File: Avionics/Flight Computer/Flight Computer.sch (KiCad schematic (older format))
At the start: 24 parts, among them U6 LP5521YQ

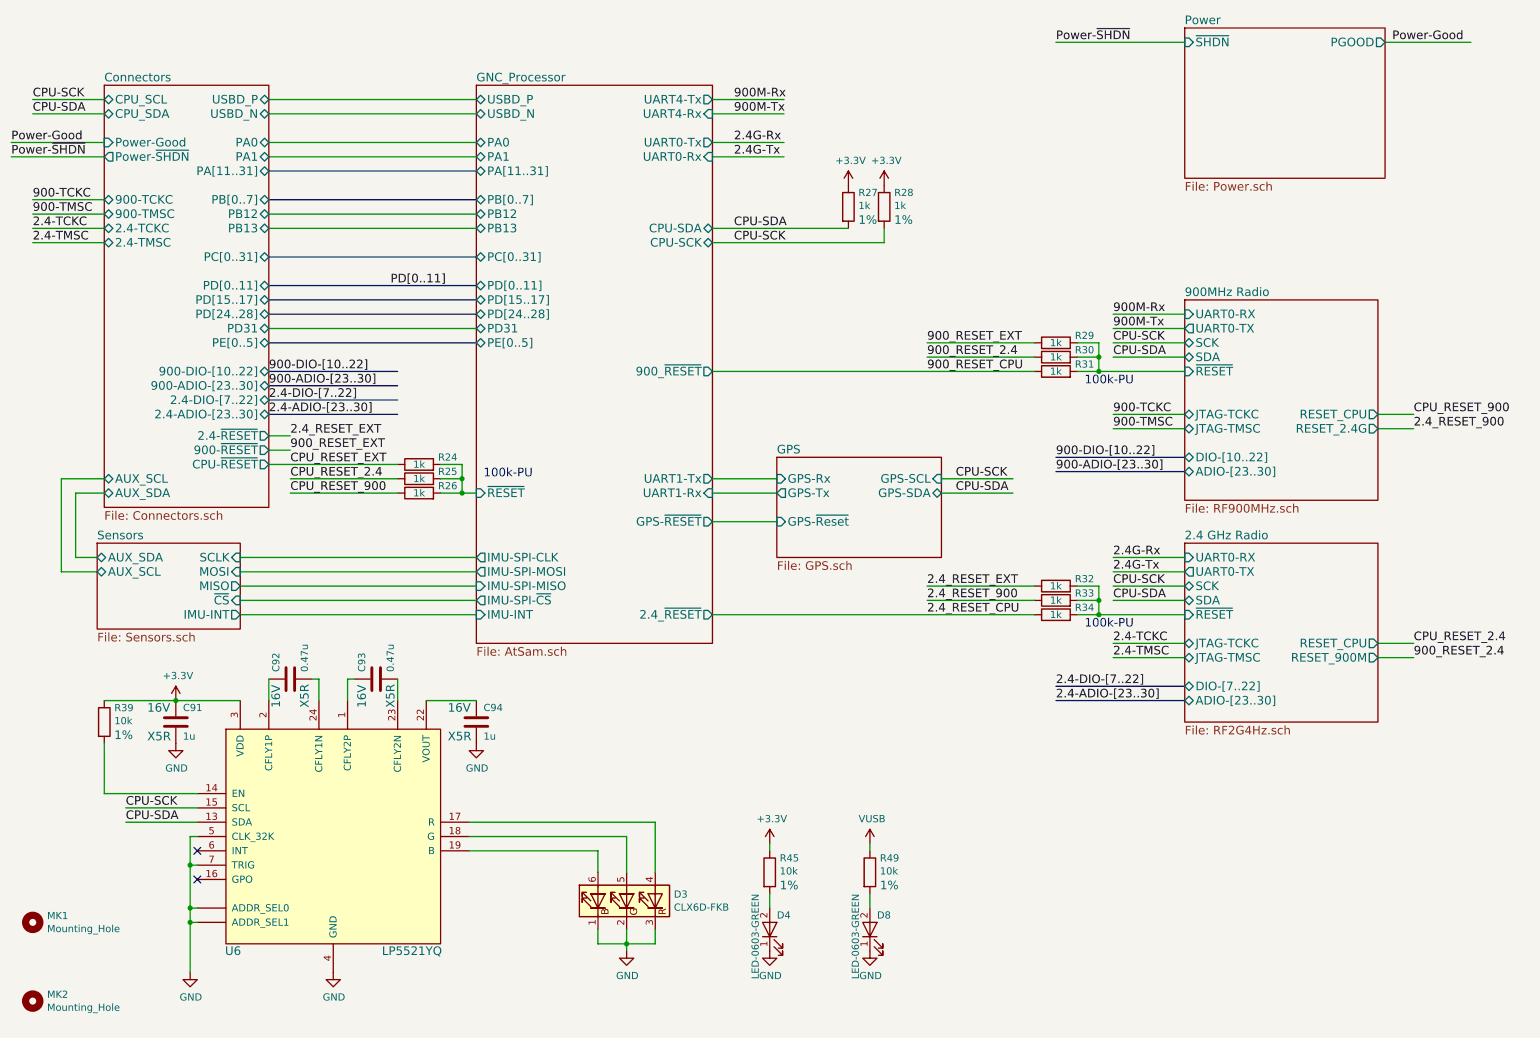
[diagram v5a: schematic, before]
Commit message: Added option resistors for IMU to be connected to radio chips via I2C
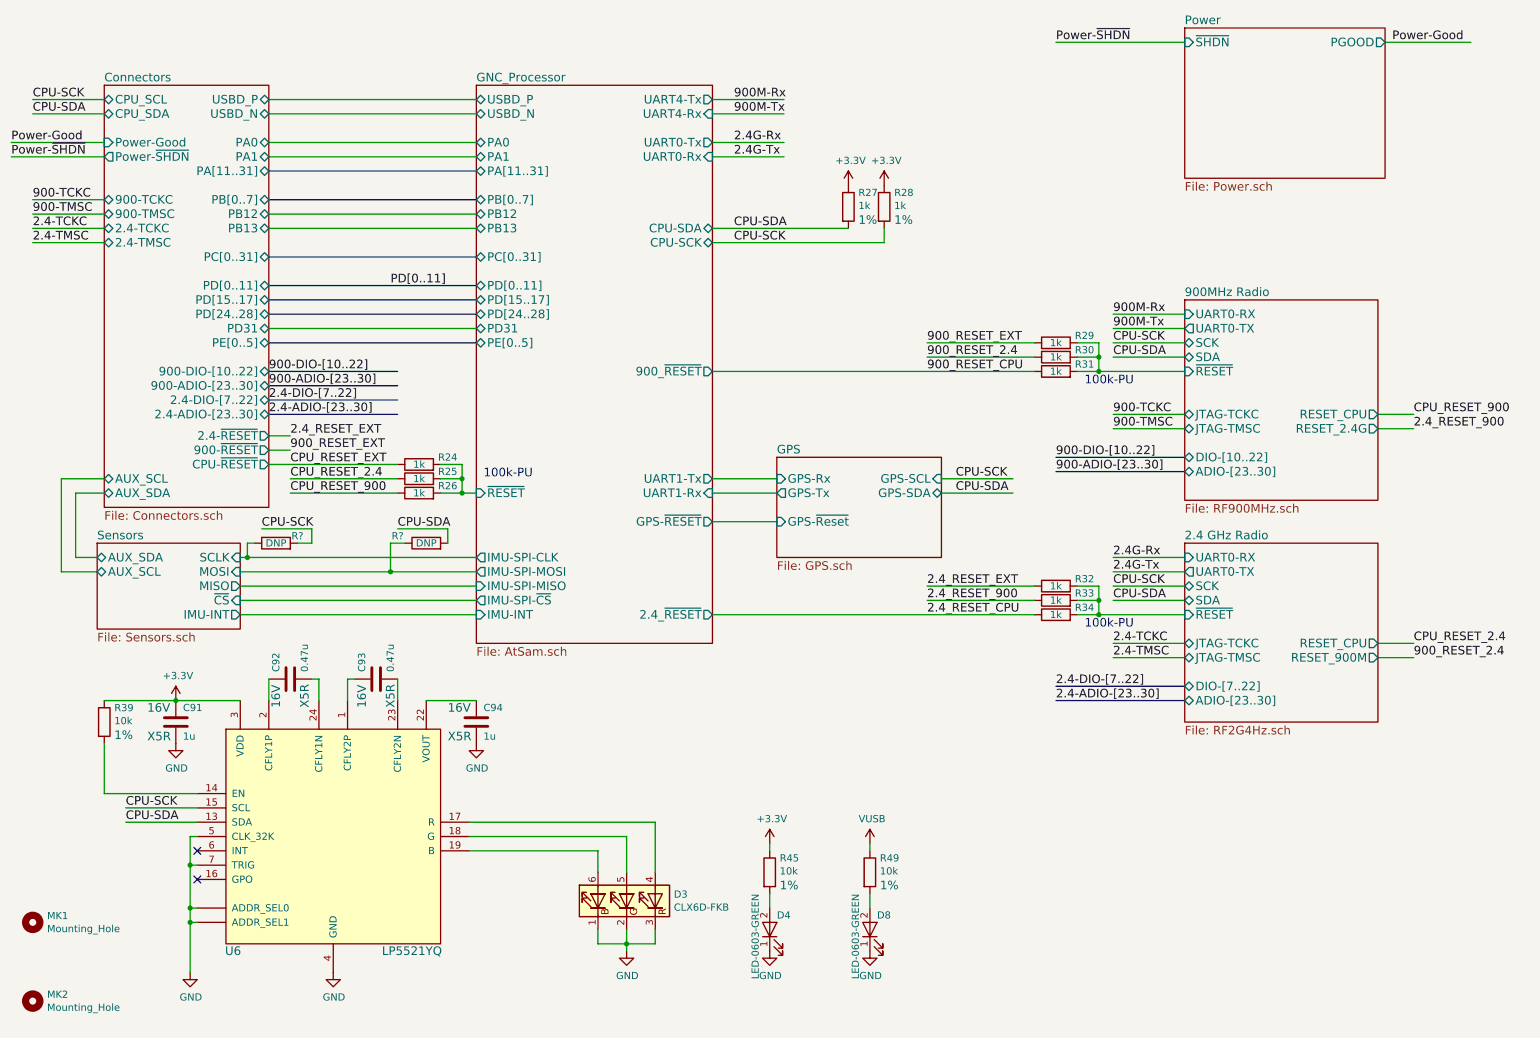
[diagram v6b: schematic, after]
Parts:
- added R? (x2): DNP, Resistors_SMD:R_0402, symbol R
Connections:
- wire segments 110 -> 133
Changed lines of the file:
@@
 	5450 2300 6650 2300
 Wire Wire Line
-	2150 4500 3800 4500
-Wire Wire Line
-	3800 4600 2150 4600
+	2150 4500 2200 4500
+Wire Wire Line
+	2200 4500 3800 4500
+Wire Wire Line
+	3800 4600 3200 4600
+Wire Wire Line
+	3200 4600 2150 4600
 Wire Wire Line
 	2150 4700 3800 4700
@@
 	6650 2300 6650 2200
 Wire Wire Line
-	3550 4050 3800 4050
+	3550 4050 3700 4050
+Wire Wire Line
+	3700 4050 3800 4050
 Wire Wire Line
 	3550 3950 3700 3950
 Wire Wire Line
-	3700 3850 3700 4050
+	3700 3850 3700 3950
+Wire Wire Line
+	3700 3950 3700 4050
 Connection ~ 3700 4050
 Wire Wire Line
@@
 	10100 5200 10350 5200
 Wire Wire Line
-	8000 4900 8750 4900
+	8000 4900 8150 4900
+Wire Wire Line
+	8150 4900 8750 4900
 Wire Wire Line
 	8000 4800 8150 4800
 Wire Wire Line
-	8150 4700 8150 4900
+	8150 4700 8150 4800
+Wire Wire Line
+	8150 4800 8150 4900
 Connection ~ 8150 4900
 Wire Wire Line
@@
 	7850 3900 8750 3900
 Wire Wire Line
-	8000 3200 8750 3200
+	8000 3200 8150 3200
+Wire Wire Line
+	8150 3200 8750 3200
 Wire Wire Line
 	8000 3100 8150 3100
 Wire Wire Line
-	8150 3000 8150 3200
+	8150 3000 8150 3100
+Wire Wire Line
+	8150 3100 8150 3200
 Connection ~ 8150 3200
 Wire Wire Line
@@
 	4650 7100 4650 7200
 Wire Wire Line
-	4650 7200 5050 7200
-Wire Wire Line
-	4850 7100 4850 7250
+	4650 7200 4850 7200
+Wire Wire Line
+	4850 7200 5050 7200
+Wire Wire Line
+	4850 7100 4850 7200
+Wire Wire Line
+	4850 7200 4850 7250
 Connection ~ 4850 7200
 Wire Wire Line
@@
 $EndComp
 Wire Wire Line
-	1200 5500 2150 5500
+	1200 5500 1700 5500
+Wire Wire Line
+	1700 5500 2150 5500
 $Comp
 L GND #PWR010
@@
 $EndComp
 Wire Wire Line
-	1800 6450 1800 7400
+	1800 6450 1800 6650
+Wire Wire Line
+	1800 6650 1800 6950
+Wire Wire Line
+	1800 6950 1800 7050
+Wire Wire Line
+	1800 7050 1800 7400
 Wire Wire Line
 	1800 6950 1850 6950
@@
 Wire Wire Line
 	7050 4050 7550 4050
+$Comp
+L R R?
+U 1 1 58D60CF9
+P 2400 4400
+F 0 "R?" V 2450 4250 50  0000 C CNN
+F 1 "DNP" V 2400 4400 50  0000 C CNN
+F 2 "Resistors_SMD:R_0402" V -5050 2750 50  0001 C CNN
+F 3 "" V -4770 2750 50  0001 C CNN
+F 4 "1%" V 2550 4700 60  0001 C CNN "Tolerance"
+F 5 "16V" V -4600 2750 60  0001 C CNN "Voltage"
+F 6 "0.062W" V -4500 2750 60  0001 C CNN "Power"
+F 7 "Thin Film" V -4400 2750 60  0001 C CNN "Material"
+F 8 "0402" V -4950 2750 60  0001 C CNN "Package"
+	1    2400 4400
+	0    -1   -1   0
+$EndComp
+$Comp
+L R R?
+U 1 1 58D60FCF
+P 3450 4400
+F 0 "R?" V 3500 4600 50  0000 C CNN
+F 1 "DNP" V 3450 4400 50  0000 C CNN
+F 2 "Resistors_SMD:R_0402" V -4000 2750 50  0001 C CNN
+F 3 "" V -3720 2750 50  0001 C CNN
+F 4 "1%" V 3600 4700 60  0001 C CNN "Tolerance"
+F 5 "16V" V -3550 2750 60  0001 C CNN "Voltage"
+F 6 "0.062W" V -3450 2750 60  0001 C CNN "Power"
+F 7 "Thin Film" V -3350 2750 60  0001 C CNN "Material"
+F 8 "0402" V -3900 2750 60  0001 C CNN "Package"
+	1    3450 4400
+	0    -1   -1   0
+$EndComp
+Wire Wire Line
+	2200 4500 2200 4400
+Wire Wire Line
+	2200 4400 2250 4400
+Connection ~ 2200 4500
+Wire Wire Line
+	3200 4600 3200 4400
+Wire Wire Line
+	3200 4400 3300 4400
+Connection ~ 3200 4600
+Wire Wire Line
+	3600 4400 3600 4300
+Wire Wire Line
+	3600 4300 3250 4300
+Wire Wire Line
+	2550 4400 2650 4400
+Wire Wire Line
+	2650 4400 2650 4300
+Wire Wire Line
+	2650 4300 2300 4300
+Text Label 2300 4300 0    60   ~ 0
+CPU-SCK
+Text Label 3250 4300 0    60   ~ 0
+CPU-SDA
 $EndSCHEMATC

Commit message: Added pullup to CS
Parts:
- added U10, U11: Logo, Symbols:NaviLOGO, symbol BOX1
- gave numbers to parts that had none: 2
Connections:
- wire segments 133 -> 119
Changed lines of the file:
@@
 $EndComp
 $Comp
-L +3.3V #PWR01
+L +3.3V #PWR12
 U 1 1 58BFF81C
 P 6650 1900
-F 0 "#PWR01" H 4950 -600 50  0001 C CNN
+F 0 "#PWR12" H 4950 -600 50  0001 C CNN
 F 1 "+3.3V" H 6665 2073 50  0000 C CNN
 F 2 "" H 4950 -450 50  0001 C CNN
@@
 $EndComp
 $Comp
-L +3.3V #PWR02
+L +3.3V #PWR9
 U 1 1 58BFF8E0
 P 6400 1900
-F 0 "#PWR02" H 4700 -600 50  0001 C CNN
+F 0 "#PWR9" H 4700 -600 50  0001 C CNN
 F 1 "+3.3V" H 6415 2073 50  0000 C CNN
 F 2 "" H 4700 -450 50  0001 C CNN
@@
 	5450 2300 6650 2300
 Wire Wire Line
-	2150 4500 2200 4500
-Wire Wire Line
-	2200 4500 3800 4500
-Wire Wire Line
-	3800 4600 3200 4600
-Wire Wire Line
-	3200 4600 2150 4600
+	2150 4500 3800 4500
+Wire Wire Line
+	2150 4600 3800 4600
 Wire Wire Line
 	2150 4700 3800 4700
@@
 	6650 2300 6650 2200
 Wire Wire Line
-	3550 4050 3700 4050
-Wire Wire Line
-	3700 4050 3800 4050
+	3550 4050 3800 4050
 Wire Wire Line
 	3550 3950 3700 3950
 Wire Wire Line
-	3700 3850 3700 3950
-Wire Wire Line
-	3700 3950 3700 4050
+	3700 3850 3700 4050
 Connection ~ 3700 4050
 Wire Wire Line
@@
 	10100 5200 10350 5200
 Wire Wire Line
-	8000 4900 8150 4900
-Wire Wire Line
-	8150 4900 8750 4900
+	8000 4900 8750 4900
 Wire Wire Line
 	8000 4800 8150 4800
 Wire Wire Line
-	8150 4700 8150 4800
-Wire Wire Line
-	8150 4800 8150 4900
+	8150 4700 8150 4900
 Connection ~ 8150 4900
 Wire Wire Line
@@
 	7850 3900 8750 3900
 Wire Wire Line
-	8000 3200 8150 3200
-Wire Wire Line
-	8150 3200 8750 3200
+	8000 3200 8750 3200
 Wire Wire Line
 	8000 3100 8150 3100
 Wire Wire Line
-	8150 3000 8150 3100
-Wire Wire Line
-	8150 3100 8150 3200
+	8150 3000 8150 3200
 Connection ~ 8150 3200
 Wire Wire Line
@@
 $EndComp
 $Comp
-L +3.3V #PWR03
+L +3.3V #PWR7
 U 1 1 58C47408
 P 5850 6500
-F 0 "#PWR03" H 4150 4000 50  0001 C CNN
+F 0 "#PWR7" H 4150 4000 50  0001 C CNN
 F 1 "+3.3V" H 5865 6673 50  0000 C CNN
 F 2 "" H 4150 4150 50  0001 C CNN
@@
 $EndComp
 $Comp
-L VUSB #PWR04
+L VUSB #PWR10
 U 1 1 58C492E4
 P 6550 6500
-F 0 "#PWR04" H 4550 5100 50  0001 C CNN
+F 0 "#PWR10" H 4550 5100 50  0001 C CNN
 F 1 "VUSB" H 6565 6673 50  0000 C CNN
 F 2 "" H 4550 5250 50  0001 C CNN
@@
 	5850 6550 5850 6500
 $Comp
-L GND #PWR05
+L GND #PWR8
 U 1 1 58C51AE7
 P 5850 7250
-F 0 "#PWR05" H 3250 -50 50  0001 C CNN
+F 0 "#PWR8" H 3250 -50 50  0001 C CNN
 F 1 "GND" H 5855 7077 50  0000 C CNN
 F 2 "" H 3250 200 50  0001 C CNN
@@
 $EndComp
 $Comp
-L GND #PWR06
+L GND #PWR11
 U 1 1 58C5304E
 P 6550 7250
-F 0 "#PWR06" H 3950 -50 50  0001 C CNN
+F 0 "#PWR11" H 3950 -50 50  0001 C CNN
 F 1 "GND" H 6555 7077 50  0000 C CNN
 F 2 "" H 3950 200 50  0001 C CNN
@@
 $EndComp
 $Comp
-L GND #PWR07
+L GND #PWR6
 U 1 1 58C8EC6C
 P 4850 7250
-F 0 "#PWR07" H 2250 -50 50  0001 C CNN
+F 0 "#PWR6" H 2250 -50 50  0001 C CNN
 F 1 "GND" H 4855 7077 50  0000 C CNN
 F 2 "" H 2250 200 50  0001 C CNN
@@
 $EndComp
 $Comp
-L GND #PWR08
+L GND #PWR4
 U 1 1 58C9E1E2
 P 2800 7400
-F 0 "#PWR08" H 200 100 50  0001 C CNN
+F 0 "#PWR4" H 200 100 50  0001 C CNN
 F 1 "GND" H 2805 7227 50  0000 C CNN
 F 2 "" H 200 350 50  0001 C CNN
@@
 	4650 7100 4650 7200
 Wire Wire Line
-	4650 7200 4850 7200
-Wire Wire Line
-	4850 7200 5050 7200
-Wire Wire Line
-	4850 7100 4850 7200
-Wire Wire Line
-	4850 7200 4850 7250
+	4650 7200 5050 7200
+Wire Wire Line
+	4850 7100 4850 7250
 Connection ~ 4850 7200
 Wire Wire Line
 	5050 7200 5050 7100
 $Comp
-L +3.3V #PWR09
+L +3.3V #PWR1
 U 1 1 58CA5175
 P 1700 5500
-F 0 "#PWR09" H 0   3000 50  0001 C CNN
+F 0 "#PWR1" H 0   3000 50  0001 C CNN
 F 1 "+3.3V" H 1715 5673 50  0000 C CNN
 F 2 "" H 0   3150 50  0001 C CNN
@@
 $EndComp
 Wire Wire Line
-	1200 5500 1700 5500
-Wire Wire Line
-	1700 5500 2150 5500
-$Comp
-L GND #PWR010
+	1200 5500 2150 5500
+$Comp
+L GND #PWR2
 U 1 1 58CBADE2
 P 1700 5800
-F 0 "#PWR010" H -900 -1500 50  0001 C CNN
+F 0 "#PWR2" H -900 -1500 50  0001 C CNN
 F 1 "GND" H 1705 5627 50  0000 C CNN
 F 2 "" H -900 -1250 50  0001 C CNN
@@
 $EndComp
 $Comp
-L GND #PWR011
+L GND #PWR5
 U 1 1 58CBC29D
 P 3800 5800
-F 0 "#PWR011" H 1200 -1500 50  0001 C CNN
+F 0 "#PWR5" H 1200 -1500 50  0001 C CNN
 F 1 "GND" H 3805 5627 50  0000 C CNN
 F 2 "" H 1200 -1250 50  0001 C CNN
@@
 Connection ~ 1700 5500
 $Comp
-L GND #PWR012
+L GND #PWR3
 U 1 1 58CD09F0
 P 1800 7400
-F 0 "#PWR012" H -800 100 50  0001 C CNN
+F 0 "#PWR3" H -800 100 50  0001 C CNN
 F 1 "GND" H 1805 7227 50  0000 C CNN
 F 2 "" H -800 350 50  0001 C CNN
@@
 $EndComp
 Wire Wire Line
-	1800 6450 1800 6650
-Wire Wire Line
-	1800 6650 1800 6950
-Wire Wire Line
-	1800 6950 1800 7050
-Wire Wire Line
-	1800 7050 1800 7400
+	1800 6450 1800 7400
 Wire Wire Line
 	1800 6950 1850 6950
@@
 	7050 4050 7550 4050
 $Comp
-L R R?
+L R R40
 U 1 1 58D60CF9
 P 2400 4400
-F 0 "R?" V 2450 4250 50  0000 C CNN
+F 0 "R40" V 2450 4250 50  0000 C CNN
 F 1 "DNP" V 2400 4400 50  0000 C CNN
 F 2 "Resistors_SMD:R_0402" V -5050 2750 50  0001 C CNN
@@
 $EndComp
 $Comp
-L R R?
+L R R41
 U 1 1 58D60FCF
 P 3450 4400
-F 0 "R?" V 3500 4600 50  0000 C CNN
+F 0 "R41" V 3500 4600 50  0000 C CNN
 F 1 "DNP" V 3450 4400 50  0000 C CNN
 F 2 "Resistors_SMD:R_0402" V -4000 2750 50  0001 C CNN
@@
 Text Label 3250 4300 0    60   ~ 0
 CPU-SDA
+$Comp
+L BOX1 U11
+U 1 1 58D75525
+P 7900 6300
+F 0 "U11" H 7950 6350 50  0001 C CNN
+F 1 "Logo" H 8028 6300 50  0000 L CNN
+F 2 "Symbols:NaviLOGO" H 1550 850 60  0001 C CNN
+F 3 "" H 1550 850 60  0001 C CNN
+	1    7900 6300
+	1    0    0    -1
+$EndComp
+$Comp
+L BOX1 U10
+U 1 1 58D772A7
+P 7900 6150
+F 0 "U10" H 7950 6200 50  0001 C CNN
+F 1 "Logo" H 8028 6150 50  0000 L CNN
+F 2 "Symbols:NaviLOGO" H 1550 700 60  0001 C CNN
+F 3 "" H 1550 700 60  0001 C CNN
+	1    7900 6150
+	1    0    0    -1
+$EndComp
 $EndSCHEMATC
